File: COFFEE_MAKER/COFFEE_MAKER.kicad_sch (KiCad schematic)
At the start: 55 parts, among them J1 Conn_01x03_Pin, J2 Conn_01x06, J3 Conn_01x03_Pin, J4 Screw_Terminal_01x02, J5 USB_C_Receptacle_USB2.0_16P, J6 Barrel_Jack, J7 Conn_01x04, Q1 BC850, SW5 Reset, SW6 Boot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

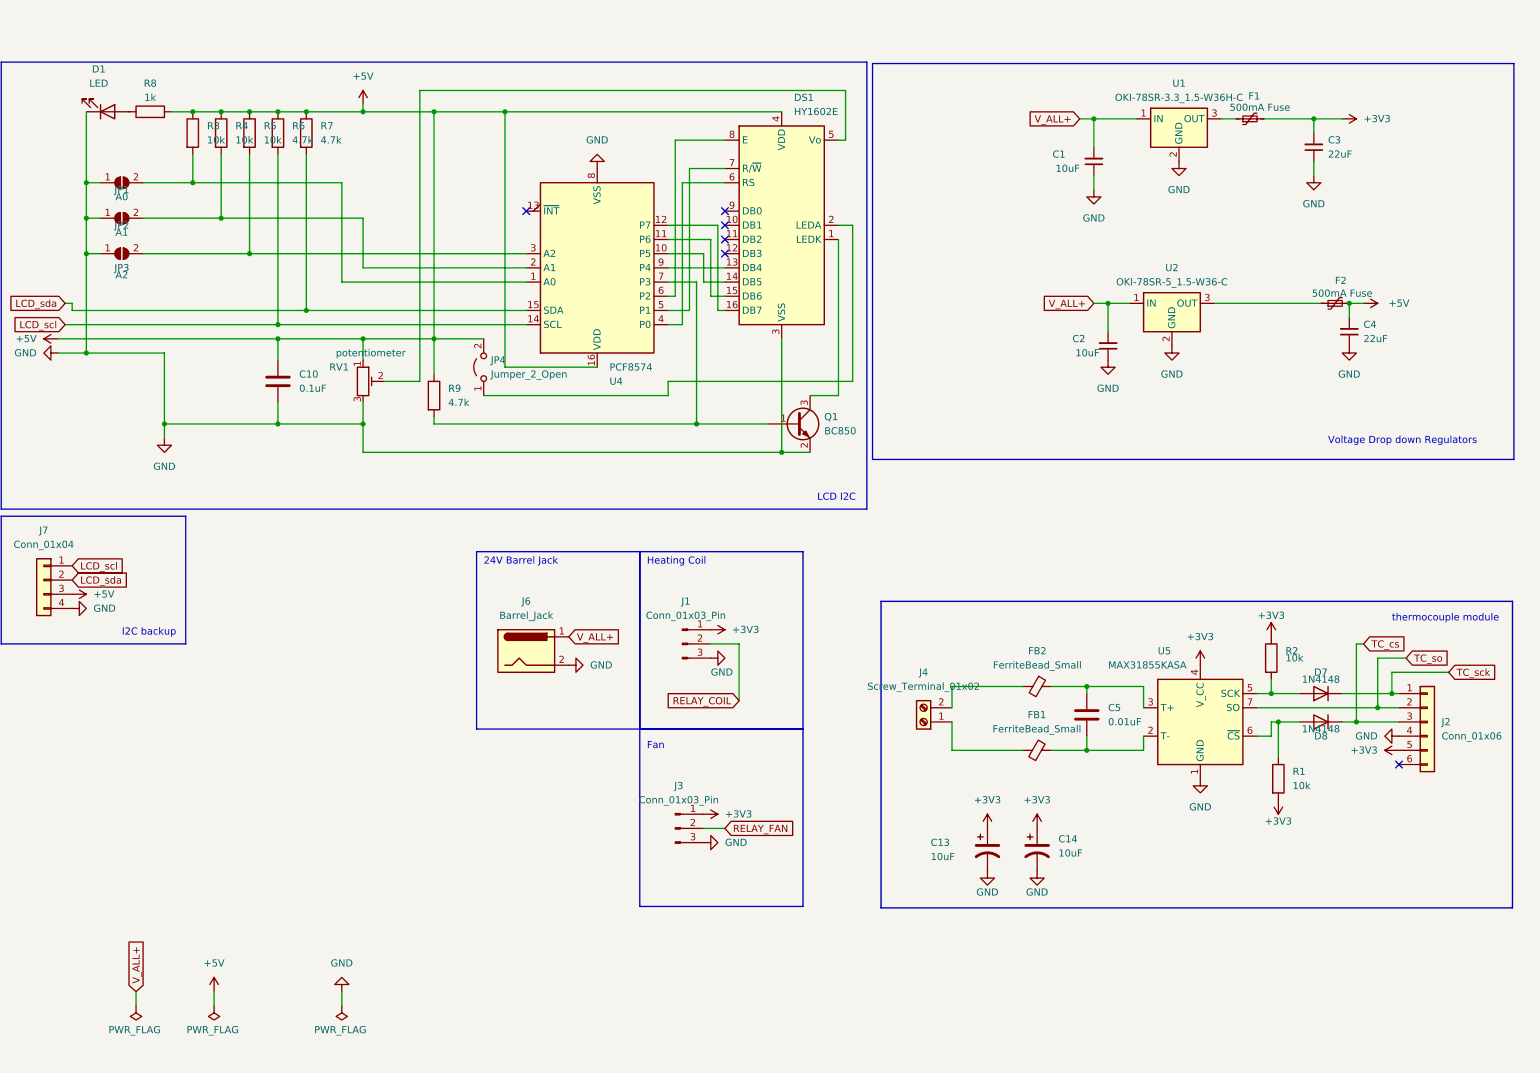
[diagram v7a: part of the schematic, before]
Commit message: pcb finalized, manufacturing folder finalized, BOM& slides in submission folder finalized
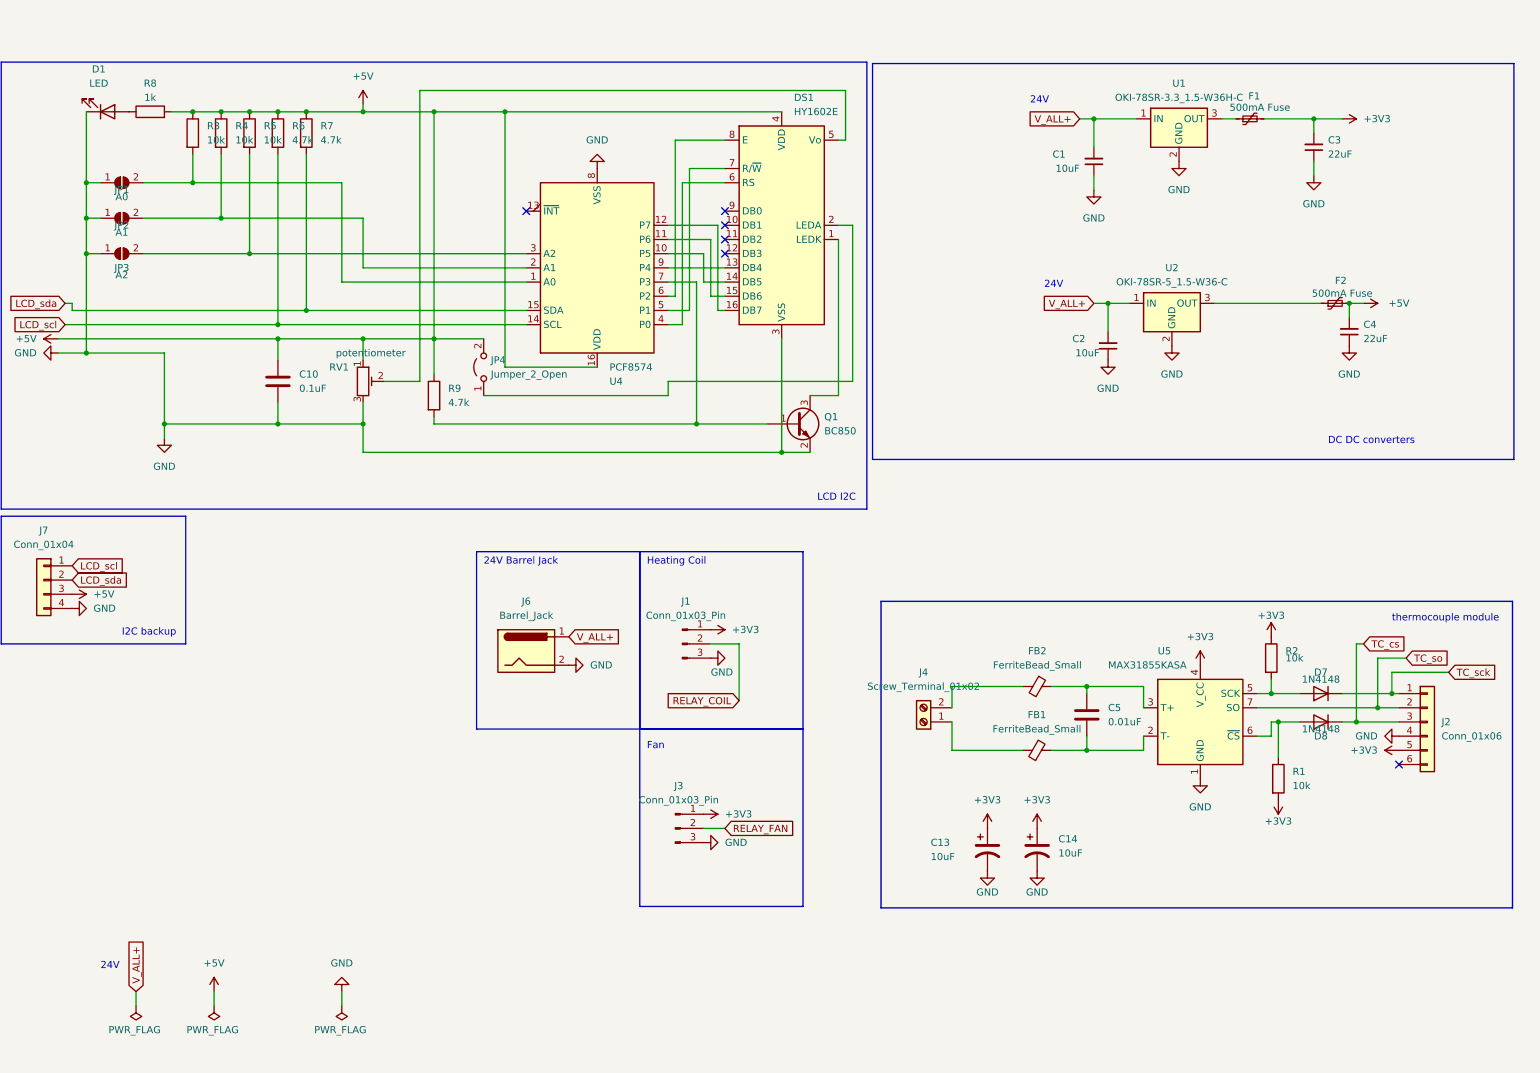
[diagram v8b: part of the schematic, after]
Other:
- note added: "24V"
- note added: "DC DC converters"
- note removed: "Voltage Drop down Regulators"
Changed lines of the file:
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@@
     (fill (type none))
+  )
+  (text "24V" (at 199.39 53.34 0)
+    (effects (font (size 1.27 1.27)) (justify left bottom))
+  )
+  (text "24V" (at 196.85 20.32 0)
+    (effects (font (size 1.27 1.27)) (justify left bottom))
   )
   (text "Heating Coil" (at 128.27 102.87 0)
@@
     (effects (font (size 1.27 1.27)) (justify left bottom))
   )
-  (text "Voltage Drop down Regulators" (at 250.19 81.28 0)
+  (text "24V" (at 30.48 175.26 0)
     (effects (font (size 1.27 1.27)) (justify left bottom))
   )
+  (text "DC DC converters" (at 250.19 81.28 0)
+    (effects (font (size 1.27 1.27)) (justify left bottom))
+  )
